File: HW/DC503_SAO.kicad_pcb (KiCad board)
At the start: 2 copper layers, 21 parts, among them J1 GS2, J2 GS2, U1 ATTINY85-20SU, X1 Badgelife_shitty_connector

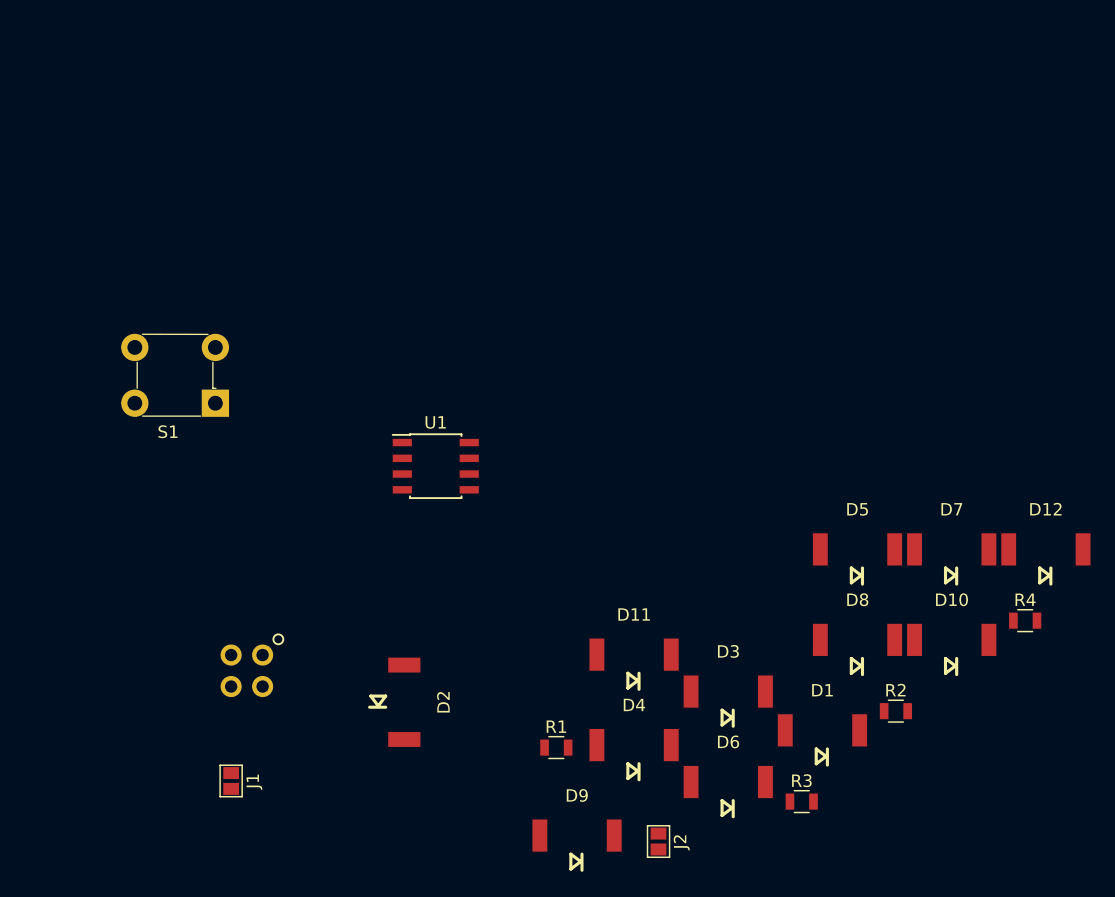
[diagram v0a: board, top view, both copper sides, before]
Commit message: added board outline
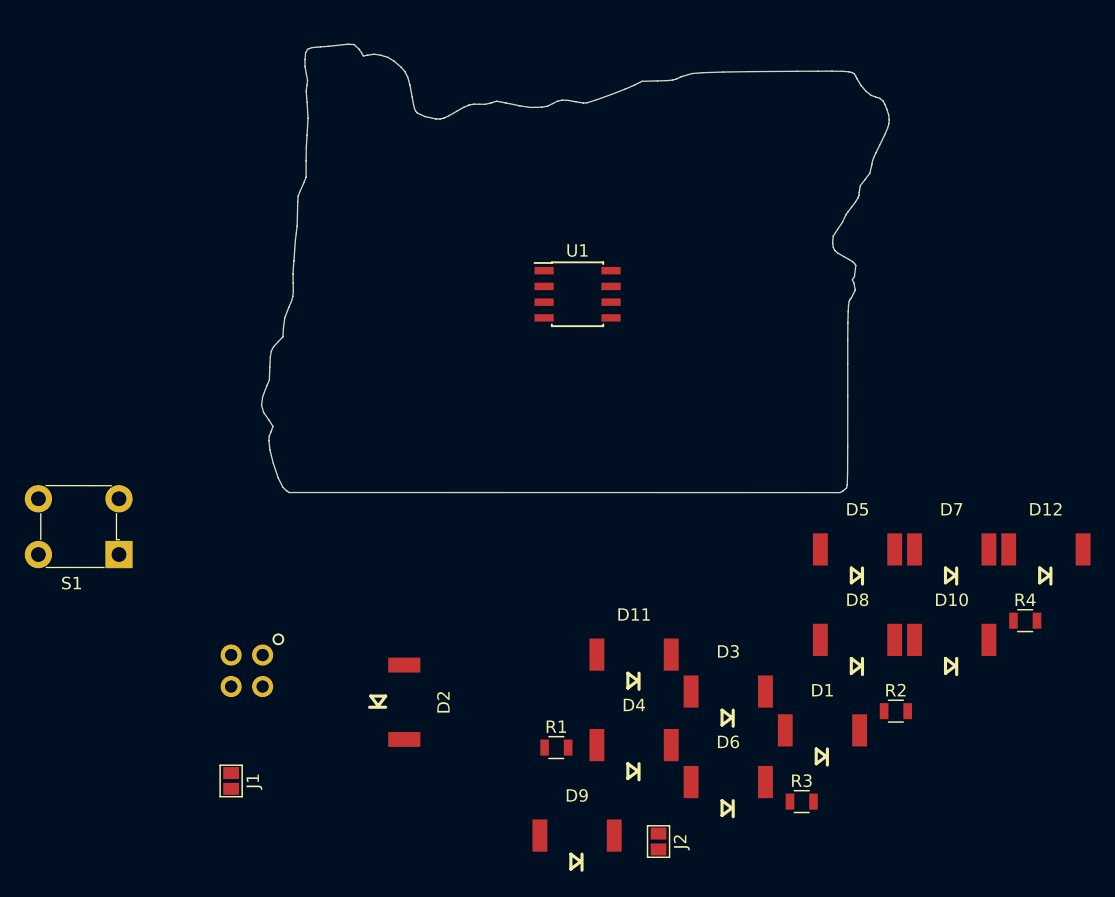
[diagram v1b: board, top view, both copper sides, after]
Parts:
- moved U1 18.0 mm to (174.0, 89.0)
- moved S1 14.5 mm to (137.0, 110.0)
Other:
- board outline added: 50.6 x 36.2 mm

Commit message: moved parts to back layer. Connected I2C pins (not ideally)
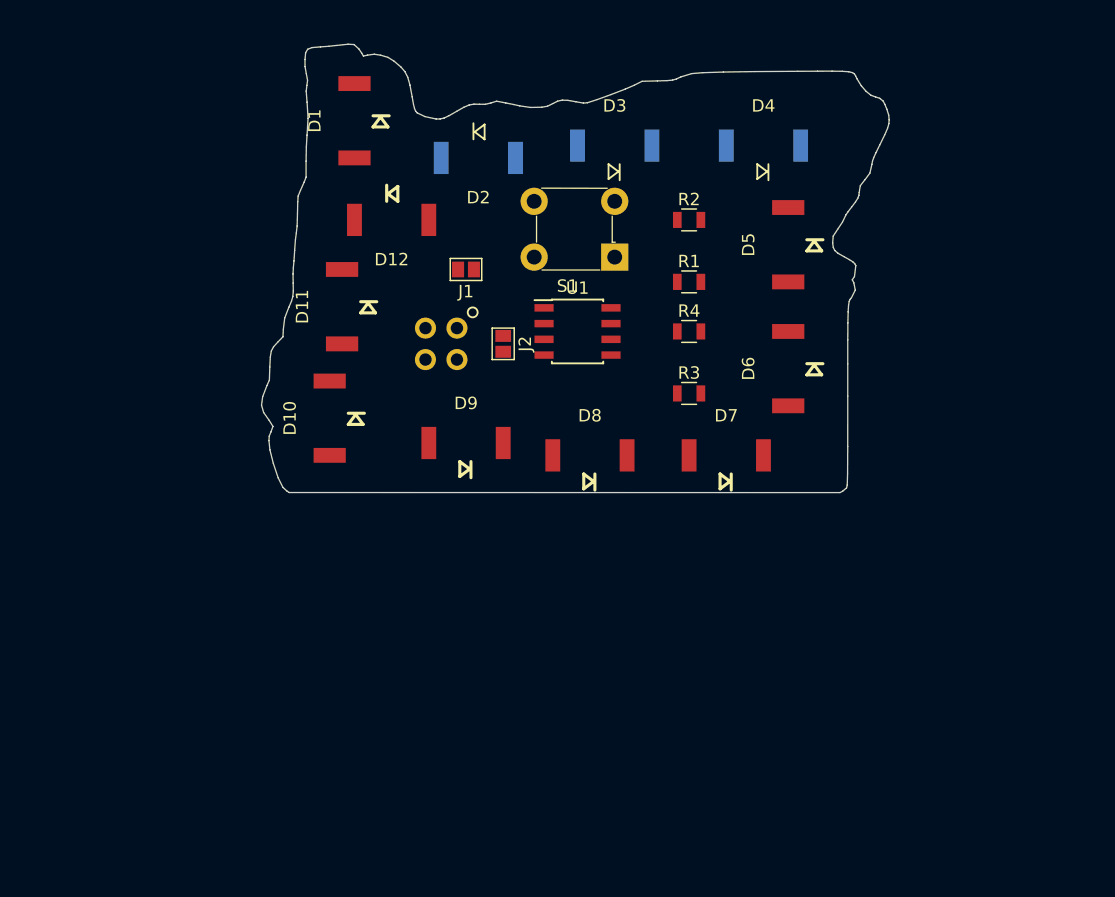
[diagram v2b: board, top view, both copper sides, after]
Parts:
- moved D1 62.0 mm to (156.0, 75.0), turned to 90 degrees
- moved D12 59.1 mm to (159.0, 83.0), turned to 180 degrees
- moved D10 53.3 mm to (154.0, 99.0), turned to 90 degrees
- moved D4 49.5 mm to (189.0, 77.0)
- moved S1 46.6 mm to (177.0, 86.0)
- moved J1 45.4 mm to (165.0, 87.0), turned to 270 degrees
- moved D3 45.0 mm to (177.0, 77.0)
- moved D2 44.3 mm to (166.0, 78.0), turned to 180 degrees
- moved R2 43.0 mm to (183.0, 83.0)
- moved J2 42.1 mm to (168.0, 93.0)
- moved R1 39.1 mm to (183.0, 88.0)
- moved D11 36.7 mm to (155.0, 90.0), turned to 90 degrees
- moved R4 35.8 mm to (183.0, 92.0)
- moved R3 34.2 mm to (183.0, 97.0)
- moved D6 33.7 mm to (191.0, 95.0), turned to 90 degrees
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
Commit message: updating stuff
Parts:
- J1, J2, R1, R2, R3, R4, U1: moved to B.Cu
- moved D2 1.30 mm to (166.1, 76.7)
- moved D10 1.26 mm to (153.6, 100.2)
- moved D1 1.22 mm to (155.0, 74.3), turned to 180 degrees
- moved D7 1.00 mm to (186.0, 101.0)
- moved D8 1.00 mm to (175.0, 101.0)
- turned J1 to 90 degrees
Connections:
- J1 pad 1: /SCL -> /ROW3
- J2 pad 1: /SDA -> /ROW1
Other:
- board size 50.6 x 36.2 mm -> 54.9 x 39.2 mm

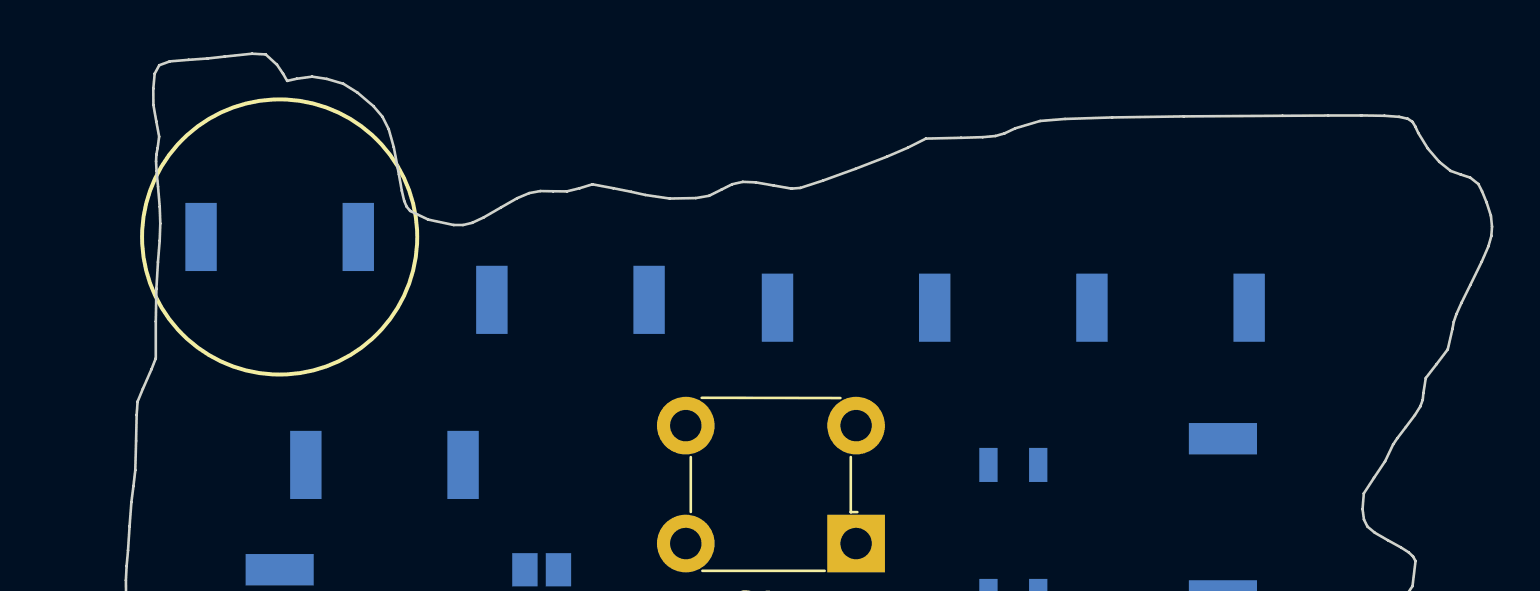
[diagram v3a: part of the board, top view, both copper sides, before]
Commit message: moving leds
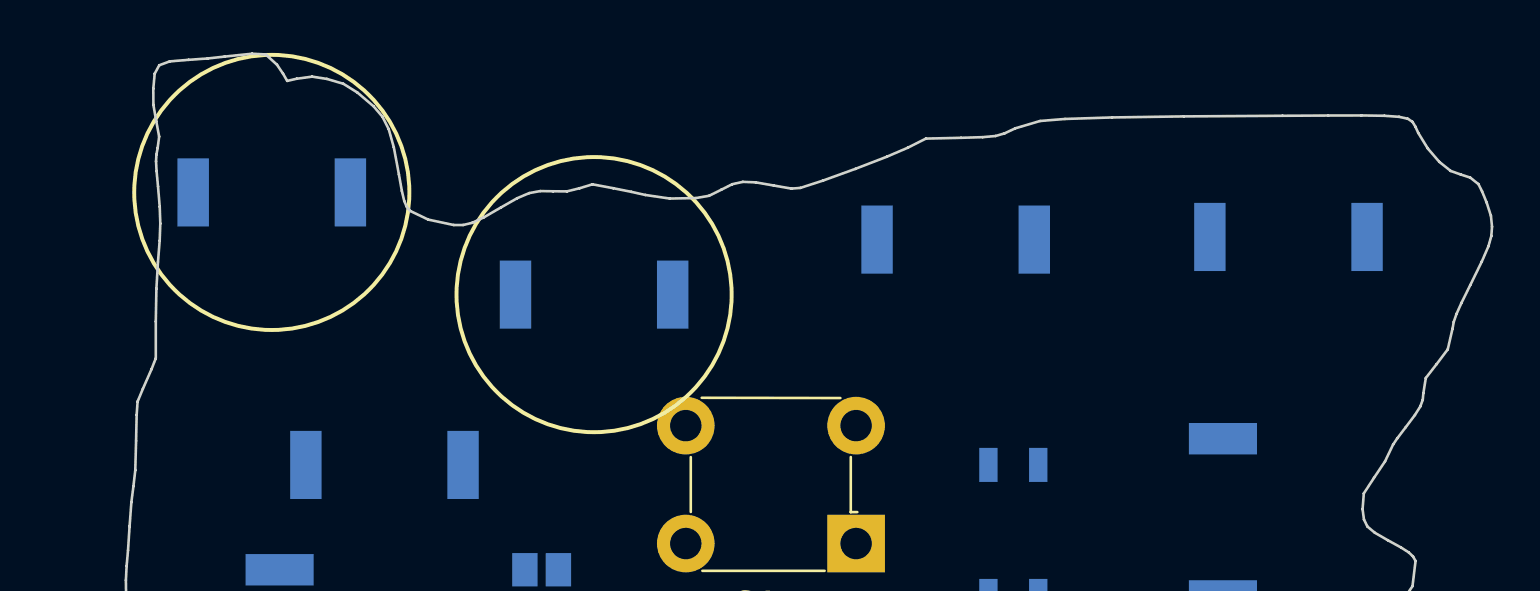
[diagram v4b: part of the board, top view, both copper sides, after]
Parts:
- moved D4 5.25 mm to (193.5, 74.3)
- moved D3 4.60 mm to (180.8, 74.4)
- moved D1 1.73 mm to (154.7, 72.6)
- moved D2 0.92 mm to (167.0, 76.5)
